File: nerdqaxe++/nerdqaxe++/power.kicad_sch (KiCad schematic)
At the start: 60 parts, among them J3 Conn_01x01, J4 Conn_01x01, U3 TPS53647, U36 MCP1824T-1202E, U6 AP3211, U7 MCP1824T-0802E

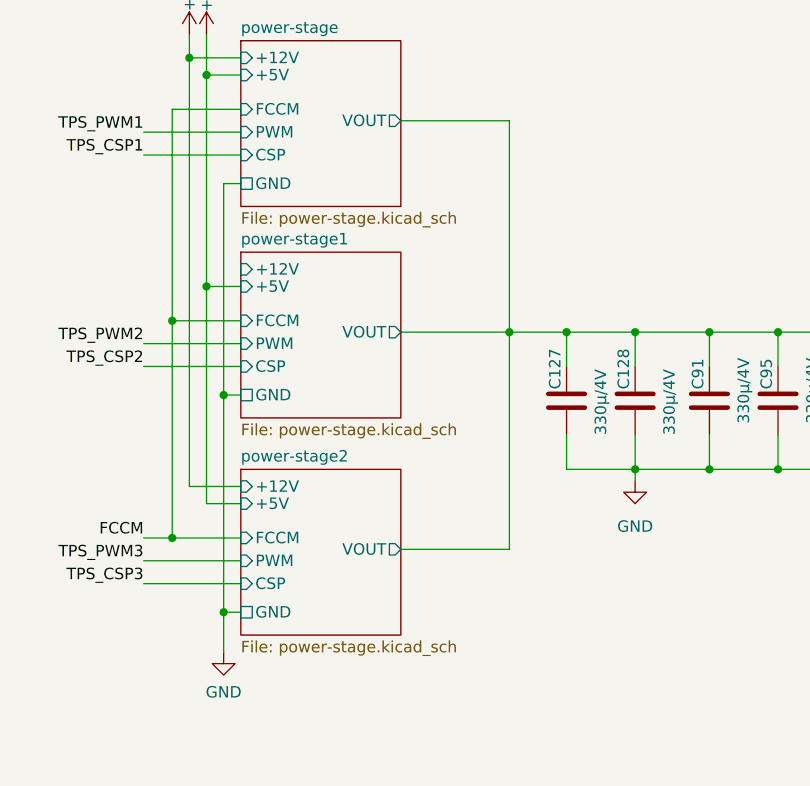
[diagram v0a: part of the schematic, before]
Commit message: fixed temp sensing connection to the buck on the ++
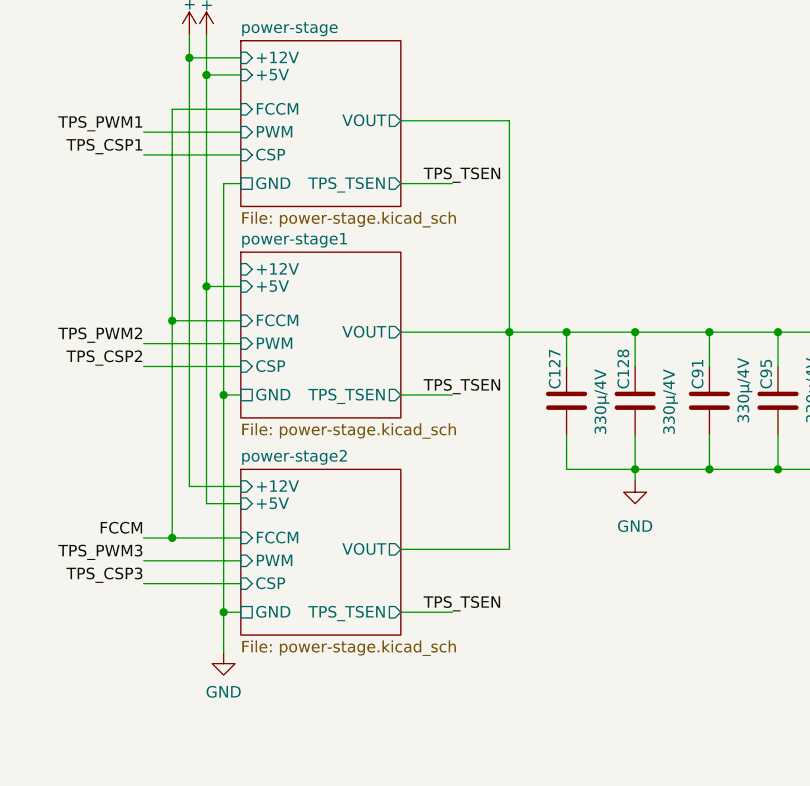
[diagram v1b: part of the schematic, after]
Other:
- sheet power-stage ports: added TPS_TSEN; removed none
- sheet power-stage1 ports: added TPS_TSEN; removed none
- sheet power-stage2 ports: added TPS_TSEN; removed none
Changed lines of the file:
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@@
 	(wire
 		(pts
+			(xy 267.97 165.1) (xy 273.685 165.1)
+		)
+		(stroke
+			(width 0)
+			(type default)
+		)
+	)
+	(wire
+		(pts
 			(xy 77.47 109.855) (xy 77.47 112.395)
 		)
@@
 	(wire
 		(pts
+			(xy 267.97 117.475) (xy 273.685 117.475)
+		)
+		(stroke
+			(width 0)
+			(type default)
+		)
+	)
+	(wire
+		(pts
 			(xy 161.29 125.095) (xy 180.34 125.095)
 		)
@@
 	(wire
 		(pts
+			(xy 267.97 140.97) (xy 273.685 140.97)
+		)
+		(stroke
+			(width 0)
+			(type default)
+		)
+	)
+	(wire
+		(pts
 			(xy 107.95 130.175) (xy 96.52 130.175)
 		)
@@
 		)
 	)
+	(label "TPS_TSEN"
+		(at 270.51 117.475 0)
+		(fields_autoplaced yes)
+		(effects
+			(font
+				(size 1.27 1.27)
+			)
+			(justify left bottom)
+		)
+	)
+	(label "TPS_TSEN"
+		(at 270.51 165.1 0)
+		(fields_autoplaced yes)
+		(effects
+			(font
+				(size 1.27 1.27)
+			)
+			(justify left bottom)
+		)
+	)
 	(label "TPS_CSP2"
 		(at 100.33 114.935 180)
@@
 		)
 	)
+	(label "TPS_TSEN"
+		(at 270.51 140.97 0)
+		(fields_autoplaced yes)
+		(effects
+			(font
+				(size 1.27 1.27)
+			)
+			(justify left bottom)
+		)
+	)
 	(label "TPS_CSP2"
 		(at 239.395 137.795 180)
@@
 			)
 		)
+		(pin "TPS_TSEN" output
+			(at 267.97 117.475 0)
+			(effects
+				(font
+					(size 1.27 1.27)
+				)
+				(justify right)
+			)
+		)
 		(instances
 			(project "nerdqaxe++"
@@
 			)
 		)
+		(pin "TPS_TSEN" output
+			(at 267.97 140.97 0)
+			(effects
+				(font
+					(size 1.27 1.27)
+				)
+				(justify right)
+			)
+		)
 		(instances
 			(project "nerdqaxe++"
@@
 			)
 		)
+		(pin "TPS_TSEN" output
+			(at 267.97 165.1 0)
+			(effects
+				(font
+					(size 1.27 1.27)
+				)
+				(justify right)
+			)
+		)

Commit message: updated 220uF on ++ to 25V
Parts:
- C135, C92: Manufacturer 875075355002 -> HHXE250ARA221MHA0G; OrderNr 732-6489-1-ND -> 565-HHXE250ARA221MHA0GCT-ND
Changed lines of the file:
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@@
 (kicad_sch
-	(version 20231120)
+	(version 20250114)
 	(generator "eeschema")
-	(generator_version "8.0")
+	(generator_version "9.0")
 	(paper "A3")
 	(title_block
@@
 		(rev "202")
 	)
+	(text "default\nOff"
+		(exclude_from_sim no)
+		(at 166.37 261.62 0)
+		(effects
+			(font
+				(size 1.27 1.27)
+			)
+		)
+	)
+	(text "for IMAX=90A"
+		(exclude_from_sim no)
+		(at 81.28 117.475 90)
+		(effects
+			(font
+				(size 1.27 1.27)
+			)
+		)
+	)
+	(text "100k = NVM"
+		(exclude_from_sim no)
+		(at 86.36 89.535 90)
+		(effects
+			(font
+				(size 1.27 1.27)
+			)
+		)
+	)
 	(junction
 		(at 242.57 156.845)
@@
 		)
 	)
-	(text "default\nOff"
-		(exclude_from_sim no)
-		(at 166.37 261.62 0)
-		(effects
-			(font
-				(size 1.27 1.27)
-			)
-		)
-	)
-	(text "for IMAX=90A"
-		(exclude_from_sim no)
-		(at 81.28 117.475 90)
-		(effects
-			(font
-				(size 1.27 1.27)
-			)
-		)
-	)
-	(text "100k = NVM"
-		(exclude_from_sim no)
-		(at 86.36 89.535 90)
-		(effects
-			(font
-				(size 1.27 1.27)
-			)
-		)
-	)
 	(label "TPS_PWM1"
 		(at 130.81 93.345 90)
-		(fields_autoplaced yes)
 		(effects
 			(font
@@
 	(label "TPS_CSP1"
 		(at 100.33 112.395 180)
-		(fields_autoplaced yes)
 		(effects
 			(font
@@
 	(label "TPS_CSP3"
 		(at 239.395 161.925 180)
-		(fields_autoplaced yes)
 		(effects
 			(font
@@
 	(label "{slash}RESET"
 		(at 168.91 130.175 0)
-		(fields_autoplaced yes)
 		(effects
 			(font
@@
 	(label "TPS_TSEN"
 		(at 125.73 93.345 90)
-		(fields_autoplaced yes)
 		(effects
 			(font
@@
 	(label "TPS_TSEN"
 		(at 270.51 117.475 0)
-		(fields_autoplaced yes)
 		(effects
 			(font
@@
 	(label "TPS_TSEN"
 		(at 270.51 165.1 0)
-		(fields_autoplaced yes)
 		(effects
 			(font
@@
 	(label "TPS_CSP2"
 		(at 100.33 114.935 180)
-		(fields_autoplaced yes)
 		(effects
 			(font
@@
 	(label "TPS_CSP3"
 		(at 100.33 117.475 180)
-		(fields_autoplaced yes)
 		(effects
 			(font
@@
 	(label "TPS_PWM2"
 		(at 133.35 93.345 90)
-		(fields_autoplaced yes)
 		(effects
 			(font
@@
 	(label "TPS_TSEN"
 		(at 270.51 140.97 0)
-		(fields_autoplaced yes)
 		(effects
 			(font
@@
 	(label "TPS_CSP2"
 		(at 239.395 137.795 180)
-		(fields_autoplaced yes)
 		(effects
 			(font
@@
 	(label "VSENSE+"
 		(at 77.47 141.605 180)
-		(fields_autoplaced yes)
 		(effects
 			(font
@@
 	(label "VSENSE-"
 		(at 337.82 172.085 0)
-		(fields_autoplaced yes)
 		(effects
 			(font
@@
 	(label "VSENSE-"
 		(at 77.47 146.685 180)
-		(fields_autoplaced yes)
 		(effects
 			(font
@@
 	(label "TPS_PWM2"
 		(at 239.395 135.255 180)
-		(fields_autoplaced yes)
 		(effects
 			(font
@@
 	(label "VSENSE+"
 		(at 337.82 168.275 0)
-		(fields_autoplaced yes)
 		(effects
 			(font
@@
 	(label "FCCM"
 		(at 128.27 92.71 90)
-		(fields_autoplaced yes)
 		(effects
 			(font
@@
 	(label "TPS_PWM3"
 		(at 135.89 93.345 90)
-		(fields_autoplaced yes)
 		(effects
 			(font
@@
 	(label "TPS_CSP1"
 		(at 239.395 114.3 180)
-		(fields_autoplaced yes)
 		(effects
 			(font
@@
 	(label "TPS_PWM1"
 		(at 239.395 111.76 180)
-		(fields_autoplaced yes)
 		(effects
 			(font
@@
 	(label "TPS_PWM3"
 		(at 239.395 159.385 180)
-		(fields_autoplaced yes)
 		(effects
 			(font
@@
 	(label "FCCM"
 		(at 239.395 156.845 180)
-		(fields_autoplaced yes)
 		(effects
 			(font
@@
 		(shape output)
 		(at 163.83 155.575 0)
-		(fields_autoplaced yes)
 		(effects
 			(font
@@
 		(shape output)
 		(at 74.93 23.495 180)
-		(fields_autoplaced yes)
 		(effects
 			(font
@@
 		(shape input)
 		(at 74.93 26.035 180)
-		(fields_autoplaced yes)
 		(effects
 			(font
@@
 		(shape input)
 		(at 165.1 122.555 0)
-		(fields_autoplaced yes)
 		(effects
 			(font
@@
 		(shape bidirectional)
 		(at 165.1 117.475 0)
-		(fields_autoplaced yes)
 		(effects
 			(font
@@
 		(shape output)
 		(at 74.93 31.115 180)
-		(fields_autoplaced yes)
 		(effects
 			(font
@@
 		(shape output)
 		(at 74.93 28.575 180)
-		(fields_autoplaced yes)
 		(effects
 			(font
@@
 		(shape output)
 		(at 74.93 36.195 180)
-		(fields_autoplaced yes)
 		(effects
 			(font
@@
 		(shape output)
 		(at 74.93 33.655 180)
-		(fields_autoplaced yes)
 		(effects
 			(font
@@
 		(shape input)
 		(at 196.85 125.095 0)
-		(fields_autoplaced yes)
 		(effects
 			(font
@@
 		(shape input)
 		(at 169.545 241.935 180)
-		(fields_autoplaced yes)
 		(effects
 			(font
@@
 			)
 		)
-		(property "Manufacturer" "875075355002"
+		(property "Manufacturer" "HHXE250ARA221MHA0G"
 			(at 189.23 34.925 0)
 			(effects
@@
 			)
 		)
-		(property "OrderNr" "732-6489-1-ND"
+		(property "OrderNr" "565-HHXE250ARA221MHA0GCT-ND"
 			(at 189.23 34.925 0)
 			(effects
@@
 			)
 		)
-		(property "Manufacturer" "875075355002"
+		(property "Manufacturer" "HHXE250ARA221MHA0G"
 			(at 179.705 34.925 0)
 			(effects
@@
 			)
 		)
-		(property "OrderNr" "732-6489-1-ND"
+		(property "OrderNr" "565-HHXE250ARA221MHA0GCT-ND"
 			(at 179.705 34.925 0)
 			(effects
@@
 		(at 250.19 101.6)
 		(size 17.78 18.415)
+		(exclude_from_sim no)
+		(in_bom yes)
+		(on_board yes)
+		(dnp no)
 		(fields_autoplaced yes)
 		(stroke
@@
 		(at 250.19 125.095)
 		(size 17.78 18.415)
+		(exclude_from_sim no)
+		(in_bom yes)
+		(on_board yes)
+		(dnp no)
 		(fields_autoplaced yes)
 		(stroke
@@
 		(at 250.19 149.225)
 		(size 17.78 18.415)
+		(exclude_from_sim no)
+		(in_bom yes)
+		(on_board yes)
+		(dnp no)
 		(fields_autoplaced yes)
 		(stroke
@@
 		)
 	)
+	(embedded_fonts no)
 )

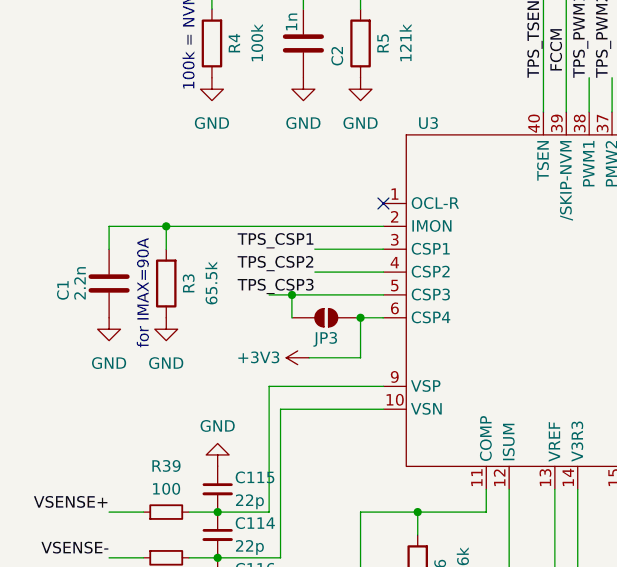
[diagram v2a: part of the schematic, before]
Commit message: fixed wrong value
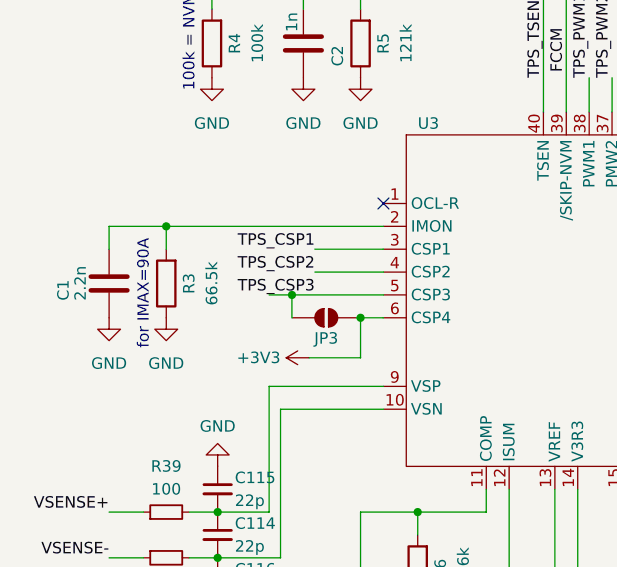
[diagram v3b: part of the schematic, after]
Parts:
- R3: value 65.5k -> 66.5k
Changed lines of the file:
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@@
 			)
 		)
-		(property "Value" "65.5k"
+		(property "Value" "66.5k"
 			(at 88.9 116.205 90)
 			(effects

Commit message: rev5.1.1
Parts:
- C1: Distributor (none) -> D; Manufacturer (none) -> C0805C222J2GACTU; OrderNr (none) -> 399-17628-1-ND; temp-coefficient (none) -> C0G
- C100, C119, C120: value 10µ -> 10µ/25V; Manufacturer C2012X5R1E106K125AB -> GRM21BZ71E106KE15L; OrderNr 445-5984-1-ND -> 490-GRM21BZ71E106KE15LCT-ND; temp-coefficient (none) -> X7R
- C101, C107: Distributor (none) -> D; Manufacturer (none) -> C0805C104K5RACTU; OrderNr (none) -> 399-C0805C104K5RACTUCT-ND; temp-coefficient (none) -> X7R
- C104: Distributor (none) -> D; Manufacturer (none) -> C0805C103J1GECTU; OrderNr (none) -> 399-C0805C103J1GECTUCT-ND; temp-coefficient (none) -> C0G
- C105, C108, C6, C8: value 1µ -> 1µ/25V; Distributor (none) -> D; Manufacturer (none) -> CL21B105KBFNNNE; OrderNr (none) -> 1276-1029-1-ND; temp-coefficient (none) -> X7R
- C106: value 22µ/16V -> 22µ/25V; footprint Capacitor_SMD:C_1206_3216Metric -> Capacitor_SMD:C_1210_3225Metric; Distributor (none) -> D; Manufacturer (none) -> CL32B226KAJNNNE; OrderNr (none) -> 1276-3392-1-ND; temp-coefficient (none) -> X7R
- C114, C115, C116: Distributor (none) -> D; Manufacturer (none) -> CL21C220JBANFNC; OrderNr (none) -> 1276-2606-1-ND; temp-coefficient (none) -> C0G
- C127, C128, C91, C95, C97, C98, C99: temp-coefficient (none) -> X5R
- C2, C4, C9: Distributor (none) -> D; Manufacturer (none) -> C0805C102J2GECTU; OrderNr (none) -> 399-C0805C102J2GECTUCT-ND; temp-coefficient (none) -> C0G
- C3: Distributor (none) -> D; Manufacturer (none) -> C0805C120J5GACTU; OrderNr (none) -> 399-C0805C120J5GACTUCT-ND; temp-coefficient (none) -> C0G
- C5: Distributor (none) -> D; Manufacturer (none) -> CL21B334KBFNNNE; OrderNr (none) -> 1276-1123-1-ND; temp-coefficient (none) -> X7R
- C7: value 4.7µ -> 4.7µ/16V; Distributor (none) -> D; Manufacturer (none) -> GRM21BR71C475KE51K; OrderNr (none) -> 490-GRM21BR71C475KE51KCT-ND; temp-coefficient (none) -> X7R
- R1: Distributor (none) -> D; Manufacturer (none) -> CRCW080516K5FKEA; OrderNr (none) -> 541-16.5KCCT-ND
- R2: Distributor (none) -> D; Manufacturer (none) -> RC0805FR-0724K3L; OrderNr (none) -> 311-24.3KCRCT-ND
- R29, R30: Distributor (none) -> D; Manufacturer (none) -> RMCF0805ZT0R00; OrderNr (none) -> RMCF0805ZT0R00CT-ND
- R3: Distributor (none) -> D; Manufacturer (none) -> RC0805FR-0766K5L; OrderNr (none) -> 311-66.5KCRCT-ND
- R31, R37, R38: Distributor (none) -> D; Manufacturer (none) -> RMCF0805FT10K0; OrderNr (none) -> RMCF0805FT10K0CT-ND
- R32: Distributor (none) -> D; Manufacturer (none) -> RC0805FR-0784K5L; OrderNr (none) -> 311-84.5KCRCT-ND
- R34: Distributor (none) -> D; Manufacturer (none) -> RMCF0805FT16K2; OrderNr (none) -> RMCF0805FT16K2CT-ND
- R39, R40: Distributor (none) -> D; Manufacturer (none) -> RC0805FR-07100RL; OrderNr (none) -> 311-100CRCT-ND
- R4: Distributor (none) -> D; Manufacturer (none) -> RMCF0805FT100K; OrderNr (none) -> RMCF0805FT100KCT-ND
- R5: Distributor (none) -> D; Manufacturer (none) -> RMCF0805FT121K; OrderNr (none) -> RMCF0805FT121KCT-ND
- R6: Distributor (none) -> D; Manufacturer (none) -> RMCF0805FT8K06; OrderNr (none) -> RMCF0805FT8K06CT-ND
- R7: Distributor (none) -> D; Manufacturer (none) -> RC0805FR-072K55L; OrderNr (none) -> 311-2.55KCRCT-ND
